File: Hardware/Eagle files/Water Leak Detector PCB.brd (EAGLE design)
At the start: 69.5 x 74.9 mm, 28 parts, among them IC1 74AHCT125, J1 Sensor 1, J2 Sensor 2, J3 Servo

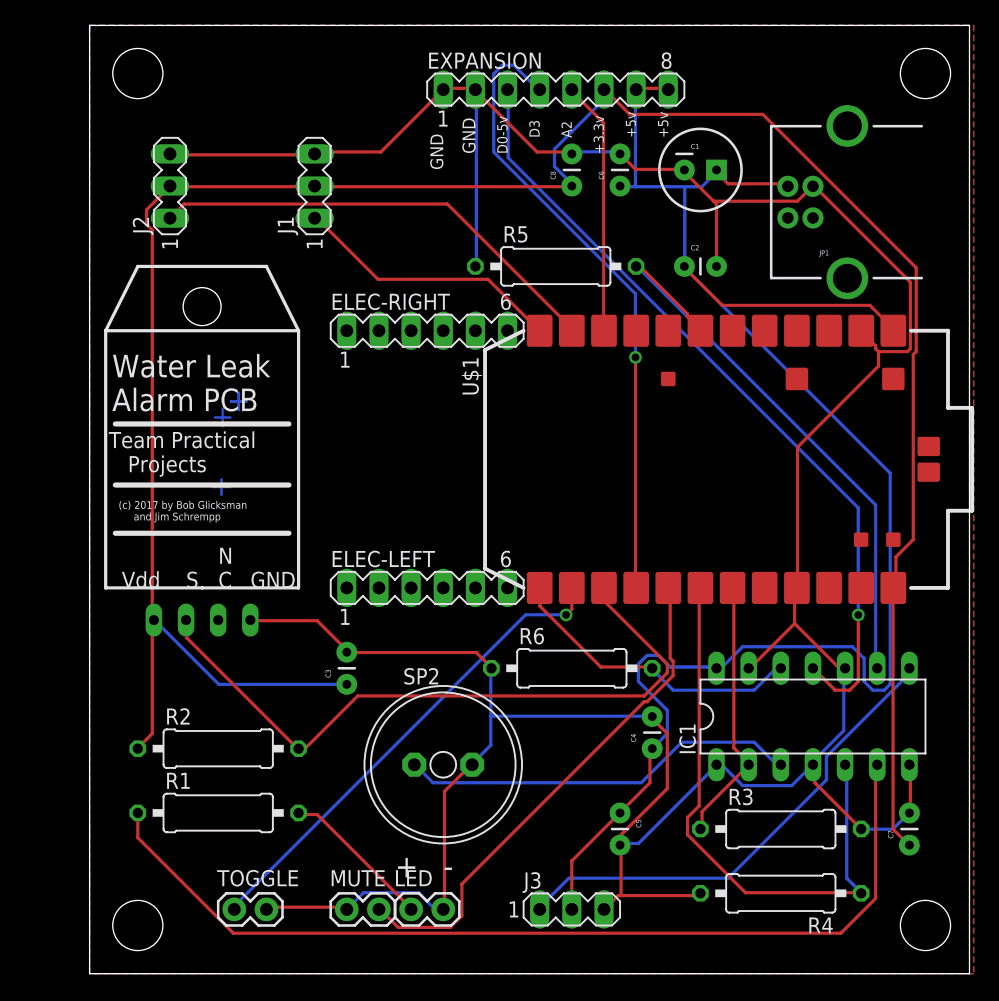
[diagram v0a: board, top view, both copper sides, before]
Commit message: Corrected and renamed files
Changed Photon to through hole version.  Changed the layout somewhat to
improve placement and routing.  Changed the names to be more
descriptive.
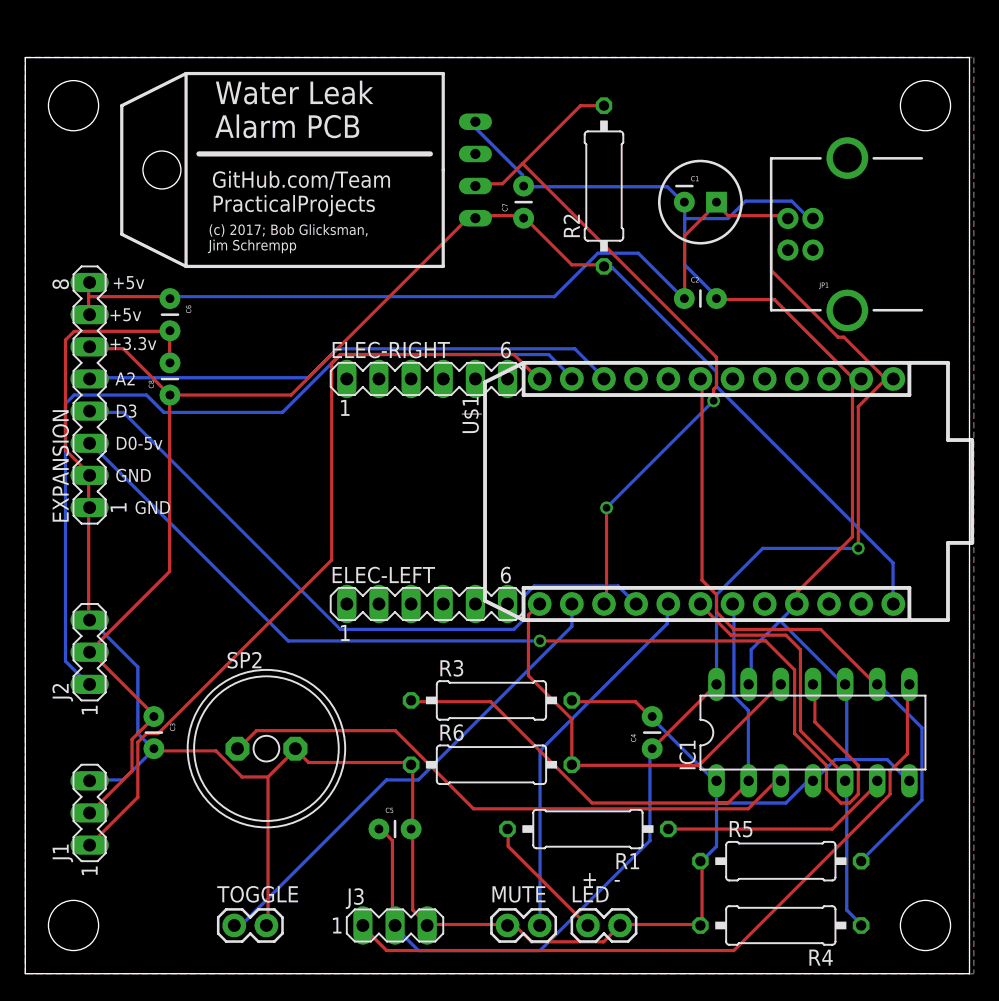
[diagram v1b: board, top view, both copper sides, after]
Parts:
- U$1: value PHOTON_SMD -> PHOTON_WITH_HEADERS; device Spark:PHOTON_SMD -> Spark:PHOTON
- moved C7 58.2 mm to (64.8, 59.7)
- moved R2 53.9 mm to (71.1, 62.2), turned to 90 degrees
- moved J1 52.6 mm to (30.5, 12.7)
- moved R5 50.2 mm to (85.1, 8.89)
- moved EXPANSION 44.0 mm to (30.5, 45.7), turned to 90 degrees
- moved U$2 41.6 mm to (61.0, 63.5), turned to 90 degrees
- moved J2 37.4 mm to (30.5, 25.4)
- moved C6 36.7 mm to (36.8, 53.3), turned to 270 degrees
- moved C8 35.8 mm to (36.8, 45.7)
- moved R1 29.2 mm to (69.8, 11.4), turned to 180 degrees
- moved R3 25.0 mm to (62.2, 21.6)
- moved C5 19.1 mm to (53.3, 11.4), turned to 0 degrees
- moved C3 15.5 mm to (35.6, 20.3), turned to 270 degrees
- moved J3 14.0 mm to (54.6, 3.81)
- moved SP2 14.0 mm to (44.5, 17.8)
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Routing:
- net N$9: track 75.2 -> 18.3 mm
- net +3.3V: track 182.4 -> 126.4 mm
- net N$3: track 21.4 -> 64.0 mm
- net N$2: track 36.5 -> 66.6 mm
- net VCC: track 137.1 -> 167.3 mm, vias 0 -> 1
- net N$15: track 62.8 -> 87.1 mm
- net N$4: track 21.2 -> 45.3 mm
- net N$16: track 20.1 -> 42.6 mm
- net N$1: track 38.5 -> 57.0 mm
- net N$6: track 31.7 -> 47.0 mm
- net N$23: track 46.3 -> 33.2 mm
- net N$11: track 40.7 -> 29.6 mm
- net N$17: track 24.0 -> 33.7 mm
- net GND: track 269.2 -> 262.8 mm
- net N$7: track 47.1 -> 51.5 mm
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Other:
- board size 69.5 x 74.9 mm -> 74.6 x 72.4 mm
- board text added: "(c) 2017; Bob Glicksman, Jim Schrempp"
- board text added: "GitHub.com/Team PracticalProjects"
- board text removed: "(c) 2017 by Bob Glicksman and Jim Schrempp"
- board text removed: "N C"
- board text removed: "S"
- board text removed: "Team Practical Projects"
- board text removed: "Vdd"

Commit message: Updated schematic
Updated schematic to show the resistor values for the components that
are on the parts list.
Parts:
- R1: value 330 ohm -> 470 ohm
- R2, R3, R4, R5, R6: value 5.6 Kohm -> 4.7 Kohm
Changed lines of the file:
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@@
 <element name="LED" library="SparkFun-Connectors" package="1X02" value="M02PTH" x="69.85" y="3.81"/>
 <element name="MUTE" library="SparkFun-Connectors" package="1X02" value="M02PTH" x="63.5" y="3.81"/>
-<element name="R1" library="rcl" package="0309/12" value="330 ohm" x="69.85" y="11.43" rot="R180"/>
-<element name="R2" library="rcl" package="0309/12" value="5.6 Kohm" x="71.12" y="62.23" rot="R90"/>
-<element name="R3" library="rcl" package="0309/12" value="5.6 Kohm" x="62.23" y="21.59"/>
-<element name="R4" library="rcl" package="0309/12" value="5.6 Kohm" x="85.09" y="3.81" rot="R180"/>
-<element name="R5" library="rcl" package="0309/12" value="5.6 Kohm" x="85.09" y="8.89"/>
-<element name="R6" library="rcl" package="0309/12" value="5.6 Kohm" x="62.23" y="16.51"/>
+<element name="R1" library="rcl" package="0309/12" value="470 ohm" x="69.85" y="11.43" rot="R180"/>
+<element name="R2" library="rcl" package="0309/12" value="4.7 Kohm" x="71.12" y="62.23" rot="R90"/>
+<element name="R3" library="rcl" package="0309/12" value="4.7 Kohm" x="62.23" y="21.59"/>
+<element name="R4" library="rcl" package="0309/12" value="4.7 Kohm" x="85.09" y="3.81" rot="R180"/>
+<element name="R5" library="rcl" package="0309/12" value="4.7 Kohm" x="85.09" y="8.89"/>
+<element name="R6" library="rcl" package="0309/12" value="4.7 Kohm" x="62.23" y="16.51"/>
 <element name="SP2" library="buzzer" package="AL11P" value="AL11P" x="44.45" y="17.78">
 <attribute name="OC_NEWARK" value="unknown" x="44.45" y="17.78" size="1.778" layer="27" display="off"/>

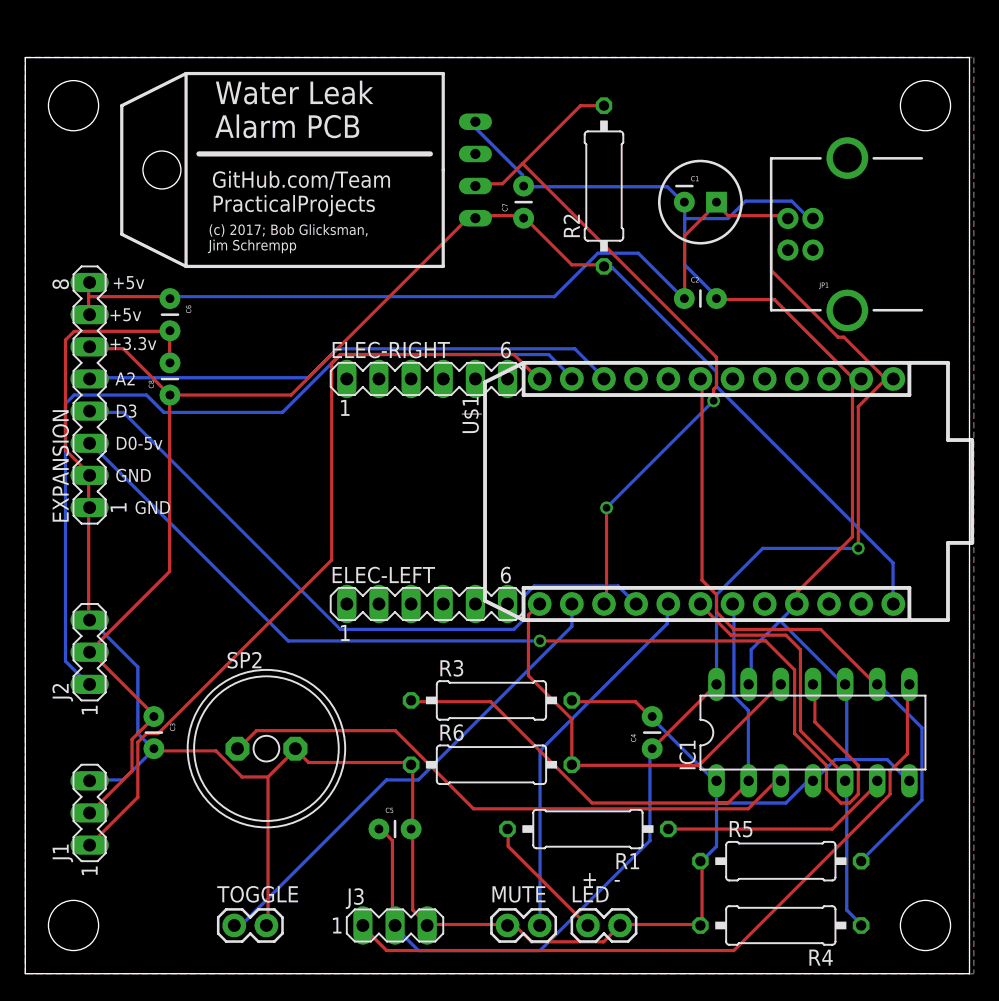
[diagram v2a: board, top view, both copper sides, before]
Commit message: pcb v2. changed buzzer. adjusted position of J1-4 to align. Added much text to top silk.
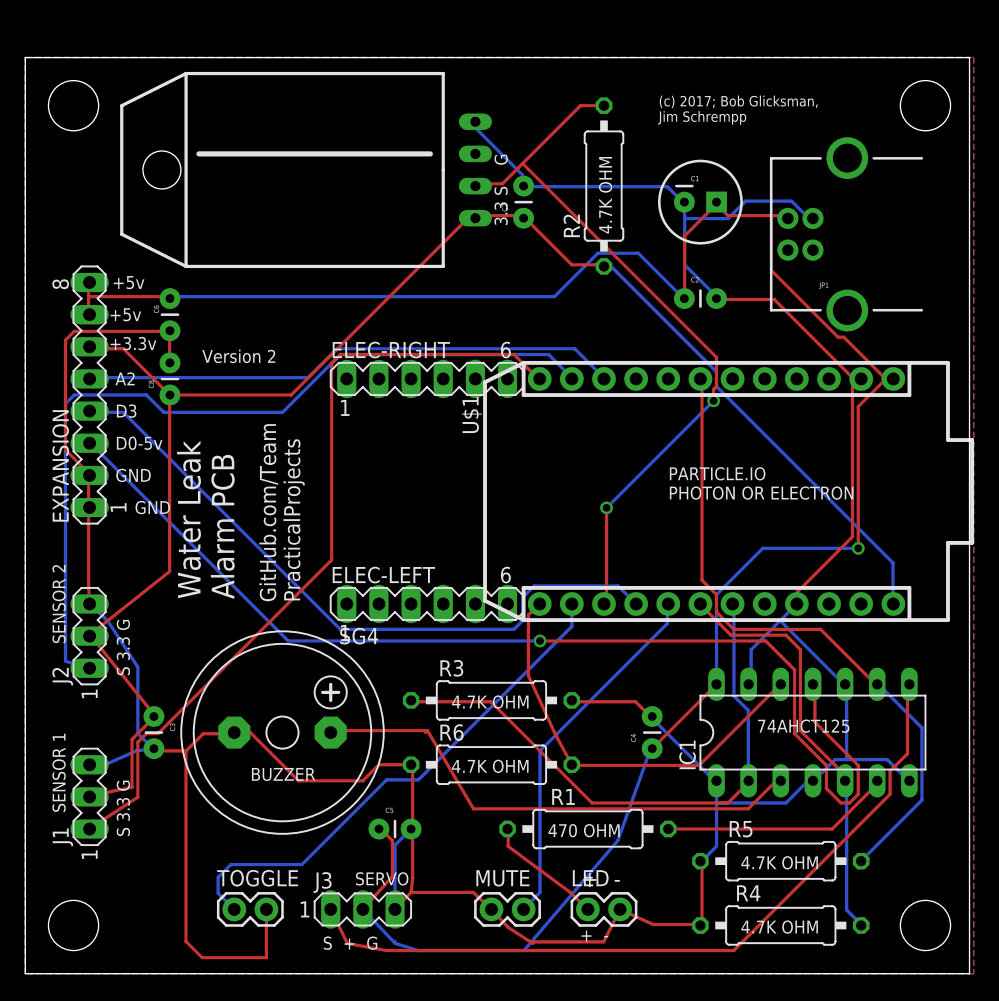
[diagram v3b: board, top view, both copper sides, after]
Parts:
- removed SP2: AL11P, buzzer:AL11P
- added SG4: (no value), buzzer:F/HMB
- J3: value Servo -> SERVO
- LED, MUTE, TOGGLE: value M02PTH -> (none)
- R1: value 470 ohm -> 470
- R2, R3, R4, R5, R6: value 4.7 Kohm -> 4.7K
- moved J3 2.84 mm to (52.1, 5.08)
- moved MUTE 1.80 mm to (62.2, 5.08)
- moved J2 1.27 mm to (30.5, 26.7)
- moved J1 1.27 mm to (30.5, 14.0)
- moved LED 1.27 mm to (69.8, 5.08)
- moved TOGGLE 1.27 mm to (41.9, 5.08)
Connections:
- net GND: now also SG4.-; no longer SP2.+
- net N$6: now also SG4.+; no longer SP2.-
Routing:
- net GND: track 262.8 -> 285.4 mm
- net N$6: track 47.0 -> 40.3 mm
- net N$1: track 57.0 -> 60.4 mm
- net N$22: track 38.2 -> 41.0 mm
- net VCC: track 167.3 -> 168.1 mm
- net N$10: track 10.3 -> 9.46 mm
- net N$3: track 64.0 -> 63.2 mm
- net N$11: track 29.6 -> 28.8 mm
- net N$2: track 66.6 -> 65.9 mm
- net N$17: track 33.7 -> 33.1 mm
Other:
- board text added: "+ -"
- board text added: "3.3 S G"
- board text added: "4.7K OHM"
- board text added: "470 OHM"
- board text added: "74AHCT125"
- board text added: "BUZZER"
- board text added: "PARTICLE.IO PHOTON OR ELECTRON"
- board text added: "S + G"
- board text added: "S 3.3 G"
- board text added: "SENSOR 1"
- board text added: "SENSOR 2"
- board text added: "SERVO"
- board text added: "Version 2"
